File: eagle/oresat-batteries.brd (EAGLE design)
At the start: 98.6 x 95.3 mm, 106 parts, among them IC1 74AHC1G08DBV, J6 J-SAMTEC-TFM-120-X1-XXX-D-RA, J7 1.27MM-SWD-CONNECTOR, Q1 CSD16340Q3, Q10 TPN4R712MD, Q11 TPN4R712MD, Q12 TPN4R712MD, Q2 CSD16340Q3, Q3 TPN4R712MD, Q4 TPN4R712MD, Q5 TPN4R712MD, Q6 TPN4R712MD, Q8 TPN4R712MD, Q9 TPN4R712MD, U1 TPS63070, U10 LTC4412, U11 MAX17055, U12 LTC4412, U13 LTC4412, U2 TCAN330, U3 BQ2970, U4 LTC4411, U5 LTC4411, U6 STM32F042K6, U7 LTC4411, U8 LTC4411, U9 LTC4412, X1 16MHZ-2.5x2mm

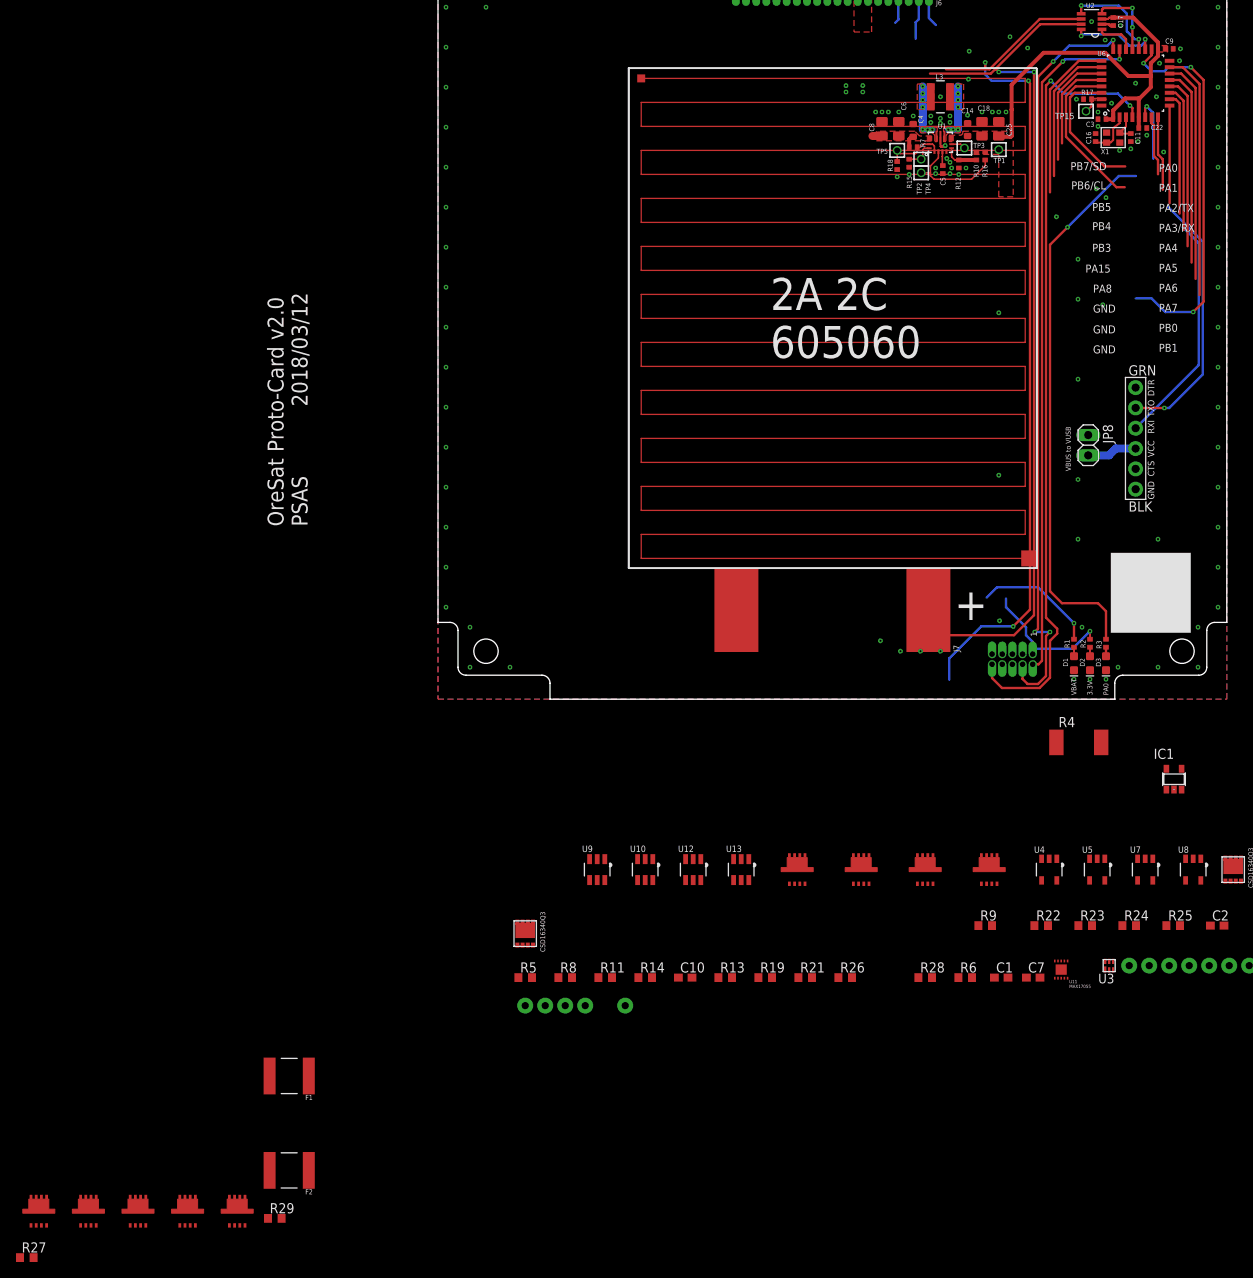
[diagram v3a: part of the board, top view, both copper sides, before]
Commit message: Assigned IO pins to circuit functions.  Finished controls for heater.
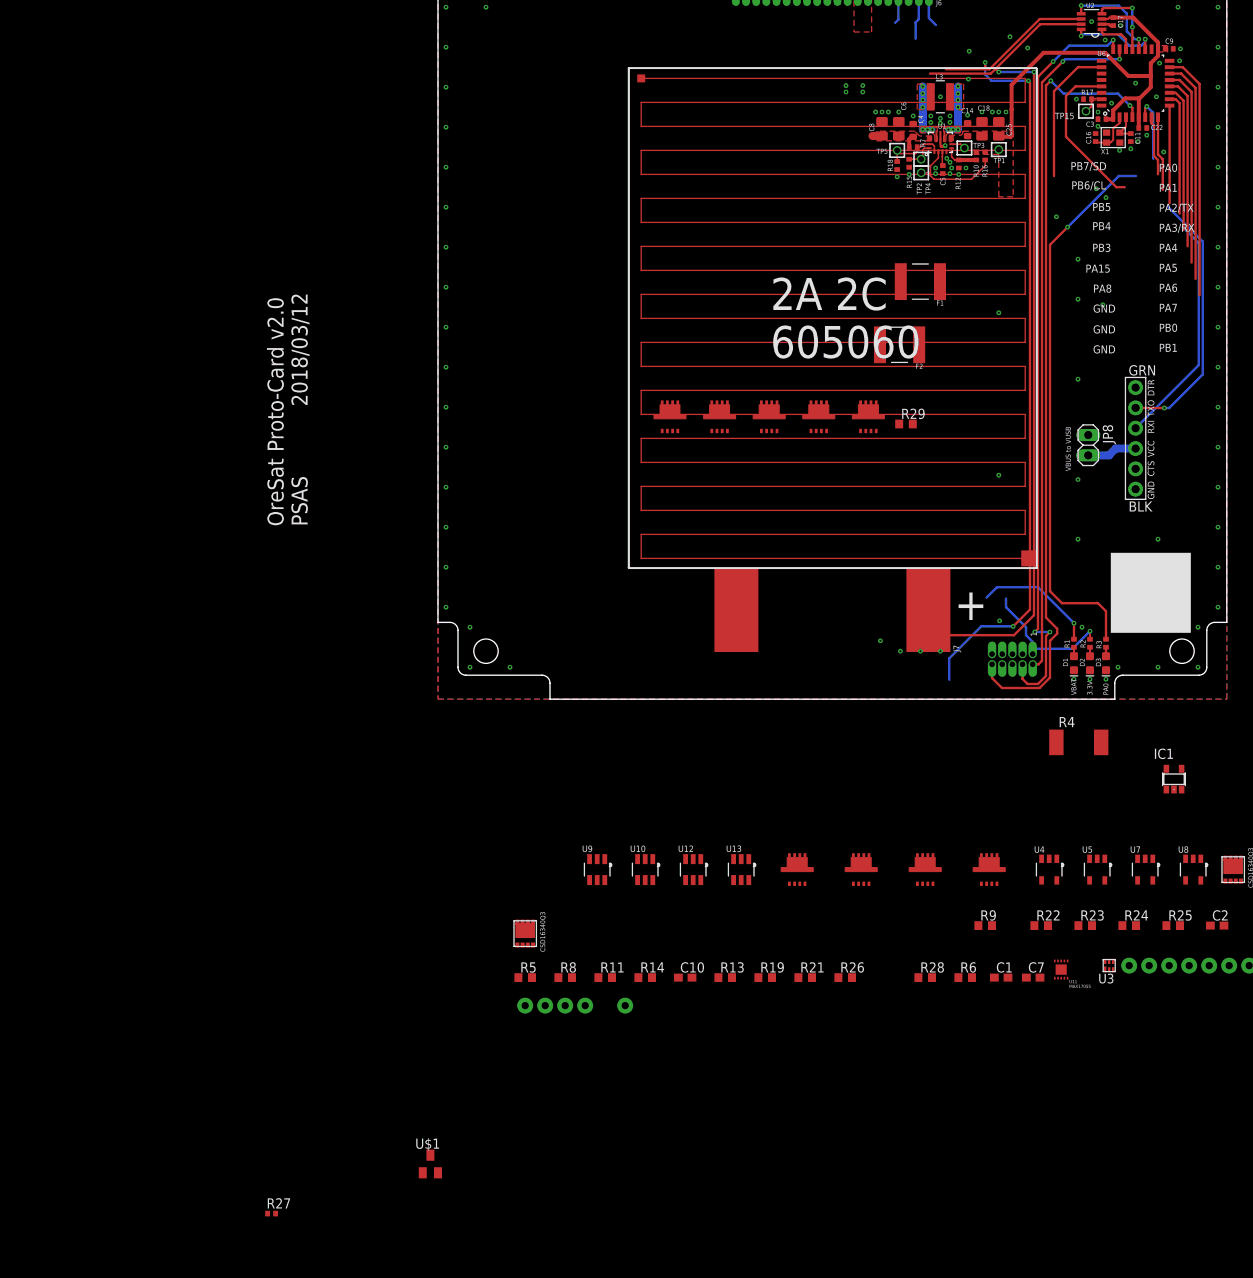
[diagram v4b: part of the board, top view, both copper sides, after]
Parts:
- added U$1: MMBT3904-TP, mmbt3904-tp:SOT23
- R27: value 100k -> 3.3k; device rcl:R0603 -> rcl:R0402
- moved F2 128.3 mm to (57.7, 44.3)
- moved F1 126.8 mm to (60.3, 52.2)
- moved R29 126.8 mm to (58.5, 34.4)
- moved Q10 126.8 mm to (41.4, 35.3)
- moved Q11 126.8 mm to (35.2, 35.3)
- moved Q12 126.8 mm to (29.0, 35.3)
- moved Q8 126.8 mm to (53.8, 35.3)
- moved Q9 126.8 mm to (47.6, 35.3)
- moved R27 31.1 mm to (-20.8, -64.3)
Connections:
- removed net !SHUTDOWN: J6.7, J6.8
- removed net N$435: Q12.1, Q12.2, Q12.3, R20.V+
- removed net PA1: U6.7
- removed net PA15: U6.25
- removed net PA4: U6.10
- removed net PA5/SPI1_SCK: U6.11
- removed net PA6/SPI1_MISO: U6.12
- removed net PA7/SPI1_MOSI: U6.13
- removed net PA8: U6.18
- removed net PB0: U6.14
- removed net PB1: U6.15
- removed net PB3: U6.26
- removed net PB4: U6.27
- removed net PB5: U6.28
- removed net PB6/SCL: U6.29
- removed net PB7/SDA: U6.30
- removed net SYSSHD: IC1.1, R14.2, TP8.P$1
- new net !SYSSHD: IC1.1, J6.7, J6.8, R14.2, TP8.P$1
- new net HEAT_FET_CTL: Q12.4, R28.1, U$1.3
- new net N$6: Q12.5, Q12.6, Q12.7, Q12.8, R20.V+
- new net N$7: R27.2, U$1.1
- net CHARGE-STAT-U4-U5: now also U6.11
- net CHARGE-STAT-U7-U8: now also U6.10
- net CHARGE_ENABLE: now also U6.15
- net DISCHARGE-STAT-U10-U13: now also U6.13
- net DISCHARGE-STAT-U9-U12: now also U6.12
- net DISCHARGE_ENABLE: now also U6.26
- net GND: now also U$1.2; no longer R27.1
- net HEAT: now also R27.1, U6.14; no longer Q12.4, R27.2, R28.1
- net MAX_IO: now also U6.7
- net SCL: now also U6.29
- net SDA: now also U6.30
- net V_BATT: now also Q12.1, Q12.2, Q12.3; no longer Q12.5, Q12.6, Q12.7, Q12.8
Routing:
- net PA8: track 48.4 -> 0.00 mm, vias 3 -> 0
- net PB1: track 31.0 -> 0.00 mm
- net CHARGE_ENABLE: track 0.00 -> 31.0 mm
- net PB0: track 27.9 -> 0.00 mm
- net HEAT: track 0.00 -> 27.9 mm
- net PA7/SPI1_MOSI: track 24.7 -> 0.00 mm
- net DISCHARGE-STAT-U10-U13: track 0.00 -> 24.7 mm
- net PA6/SPI1_MISO: track 21.5 -> 0.00 mm
- net DISCHARGE-STAT-U9-U12: track 0.00 -> 21.5 mm
- net PA15: track 20.8 -> 0.00 mm
- net SCL: track 0.00 -> 20.0 mm
- net PB6/SCL: track 20.0 -> 0.00 mm
- net PA5/SPI1_SCK: track 18.3 -> 0.00 mm
- net CHARGE-STAT-U4-U5: track 0.00 -> 18.3 mm
- net PB3: track 17.8 -> 0.00 mm
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
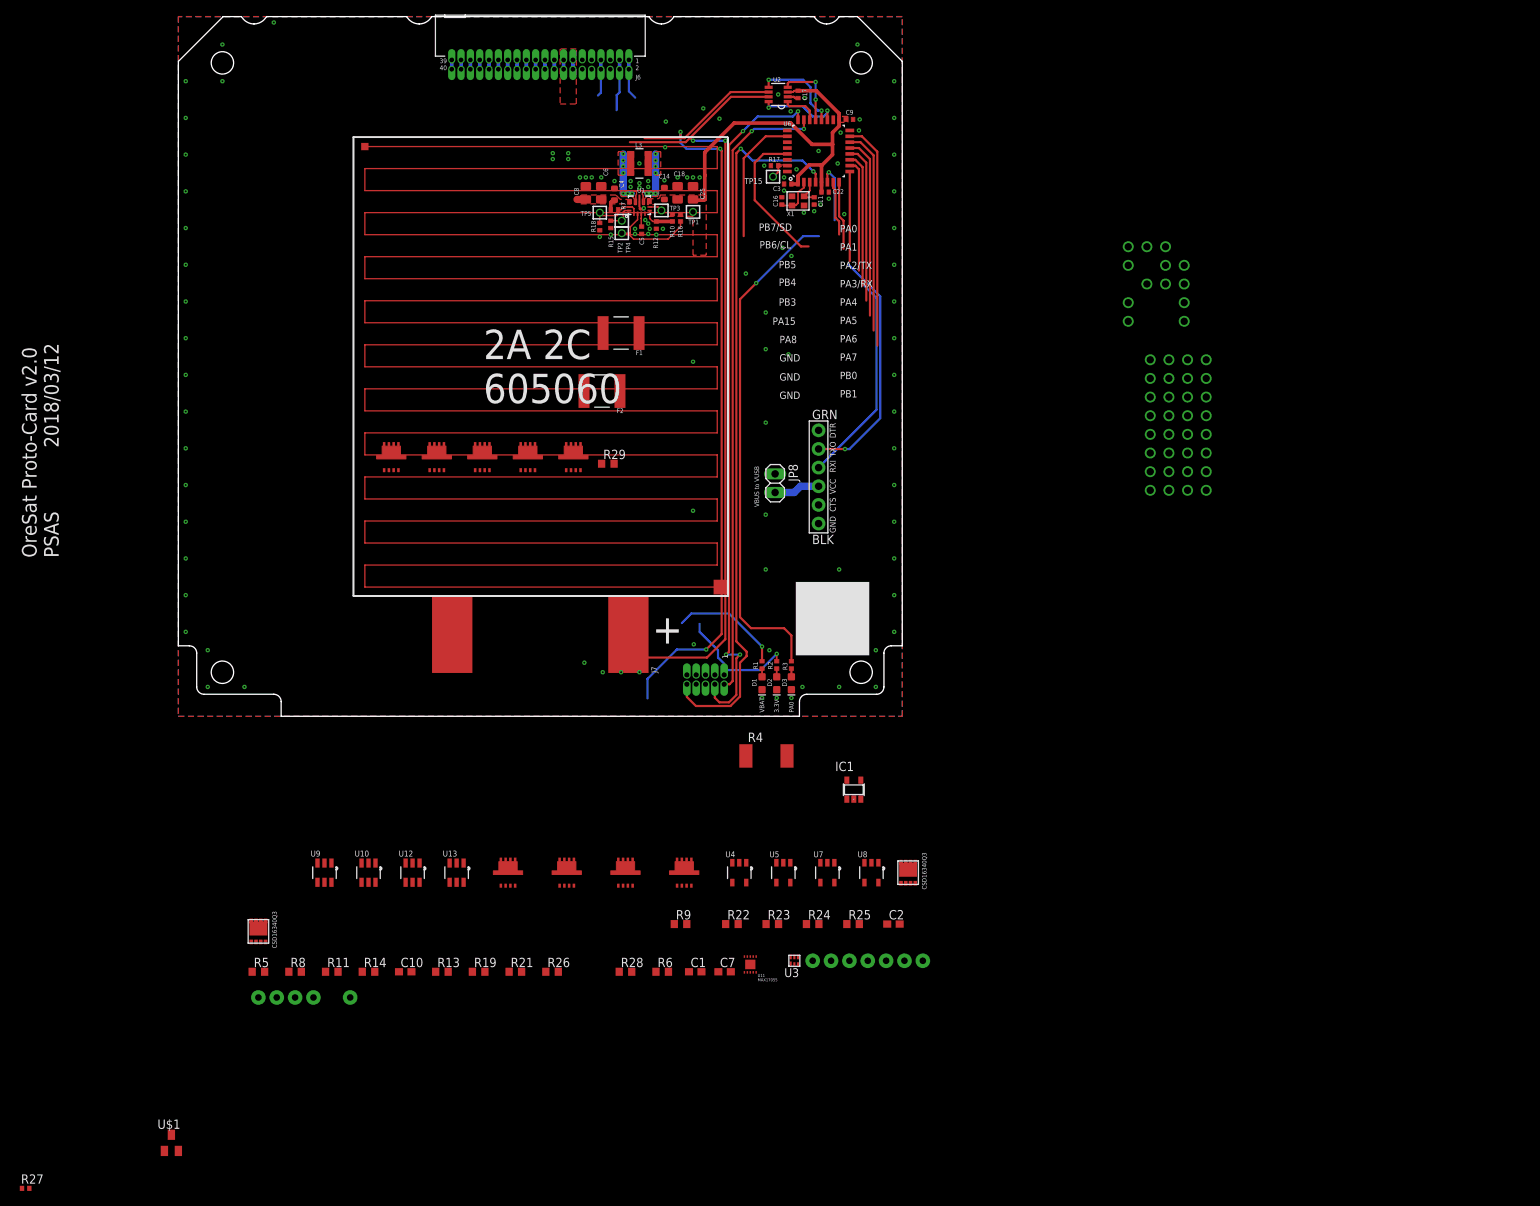
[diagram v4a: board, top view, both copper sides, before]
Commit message: Last changes to previous 1 cell battery pack. Abandoning for 2 cell packs because we're weenies.
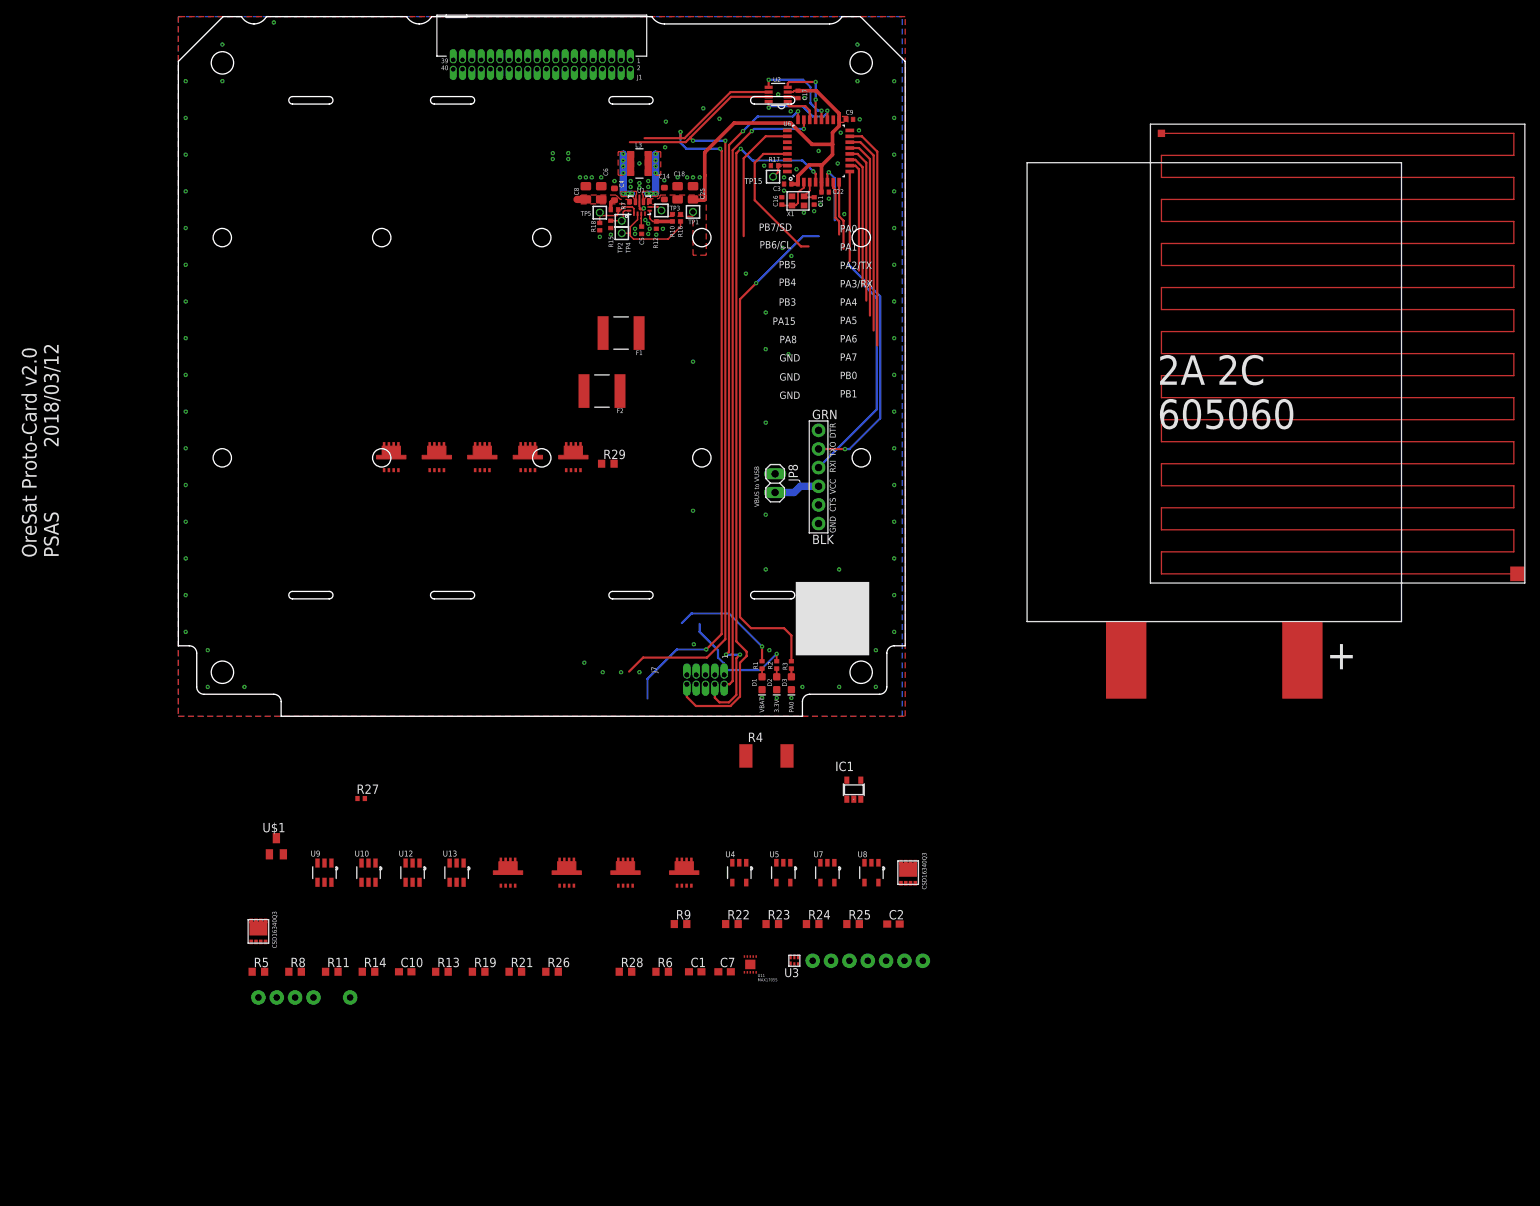
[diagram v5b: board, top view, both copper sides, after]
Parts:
- removed J6: J-SAMTEC-TFM-120-X1-XXX-D-RA, J-Samtec-TFM-120-X1-XXX-D-RA:J-SAMTEC-TFM-120-X1-XXX-D-RA
- added J1: J-SAMTEC-TFM-120-X1-XXX-D-RA, J-Samtec-TFM-120-X1-XXX-D-RA:J-SAMTEC-TFM-120-X1-XXX-D-RA
- U$2: value ORESAT-CARD-V0.5 -> (none)
- moved R20 108.5 mm to (157.9, 49.4)
- moved B1 91.9 mm to (141.1, 44.1)
- moved R27 70.1 mm to (24.9, -11.2)
- moved U$1 42.9 mm to (13.3, -17.7)
- renumbered CARD to U$2
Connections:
- net !SYSSHD: now also J1.7, J1.8; no longer J6.7, J6.8
- net CAN_H: now also J1.3, J1.4; no longer J6.3, J6.4
- net CAN_L: now also J1.1, J1.2; no longer J6.1, J6.2
- net GND: now also J1.10, J1.11, J1.12, J1.5, J1.6, J1.9; no longer J6.10, J6.11, J6.12, J6.5, J6.6, J6.9
- net SPARE1: now also J1.17, J1.18; no longer J6.17, J6.18
- net SPARE10: now also J1.35, J1.36; no longer J6.35, J6.36
- net SPARE11: now also J1.37, J1.38; no longer J6.37, J6.38
- net SPARE12: now also J1.39, J1.40; no longer J6.39, J6.40
- net SPARE2: now also J1.19, J1.20; no longer J6.19, J6.20
- net SPARE3: now also J1.21, J1.22; no longer J6.21, J6.22
- net SPARE4: now also J1.23, J1.24; no longer J6.23, J6.24
- net SPARE5: now also J1.25, J1.26; no longer J6.25, J6.26
- net SPARE6: now also J1.27, J1.28; no longer J6.27, J6.28
- net SPARE7: now also J1.29, J1.30; no longer J6.29, J6.30
- net SPARE8: now also J1.31, J1.32; no longer J6.31, J6.32
- net SPARE9: now also J1.33, J1.34; no longer J6.33, J6.34
- net VBUS: now also J1.13, J1.14, J1.15, J1.16; no longer J6.13, J6.14, J6.15, J6.16
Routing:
- net CAN_H: track 116.3 -> 109.3 mm
- net CAN_L: track 114.5 -> 109.1 mm
- net !SYSSHD: track 5.02 -> 0.00 mm
- net VBUS: track 21.2 -> 18.1 mm
- net SPARE9: track 1.27 -> 0.00 mm
- net SPARE8: track 1.27 -> 0.00 mm
- net SPARE7: track 1.27 -> 0.00 mm
- net SPARE6: track 1.27 -> 0.00 mm
- net SPARE5: track 1.27 -> 0.00 mm
- net SPARE4: track 1.27 -> 0.00 mm
- net SPARE3: track 1.27 -> 0.00 mm
- net SPARE2: track 1.27 -> 0.00 mm
- net SPARE12: track 1.27 -> 0.00 mm
- net SPARE11: track 1.27 -> 0.00 mm
- net SPARE10: track 1.27 -> 0.00 mm
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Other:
- board size 98.6 x 95.3 mm -> 99 x 95.3 mm
